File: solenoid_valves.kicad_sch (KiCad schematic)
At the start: 0 parts

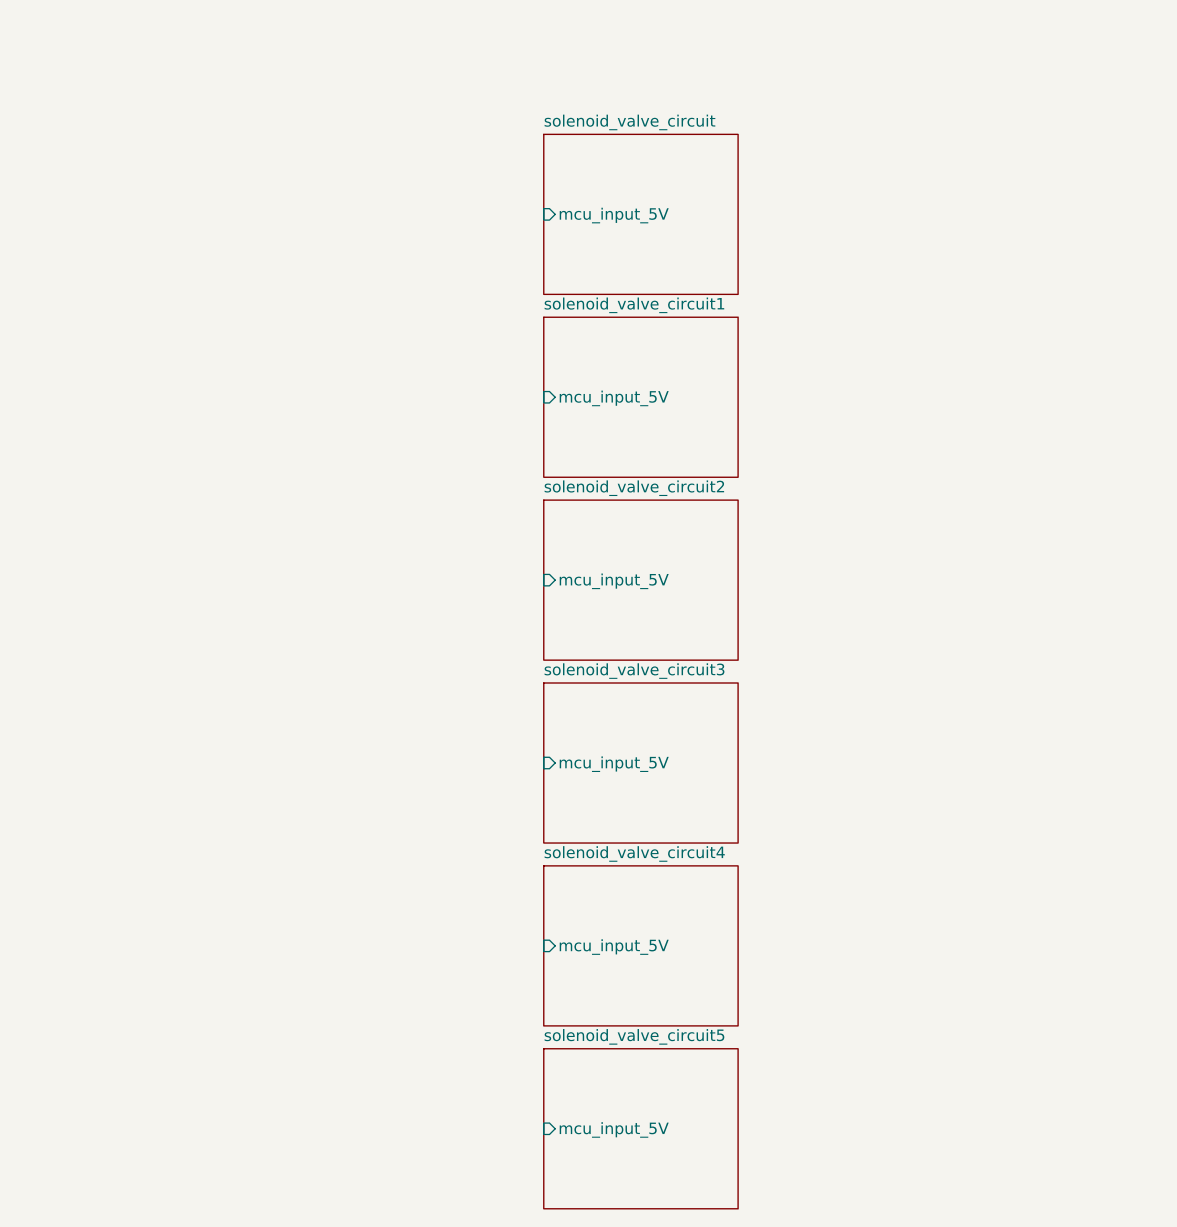
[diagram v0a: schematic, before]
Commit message: added npn in so that GPIO can be 5V or roughly 0V
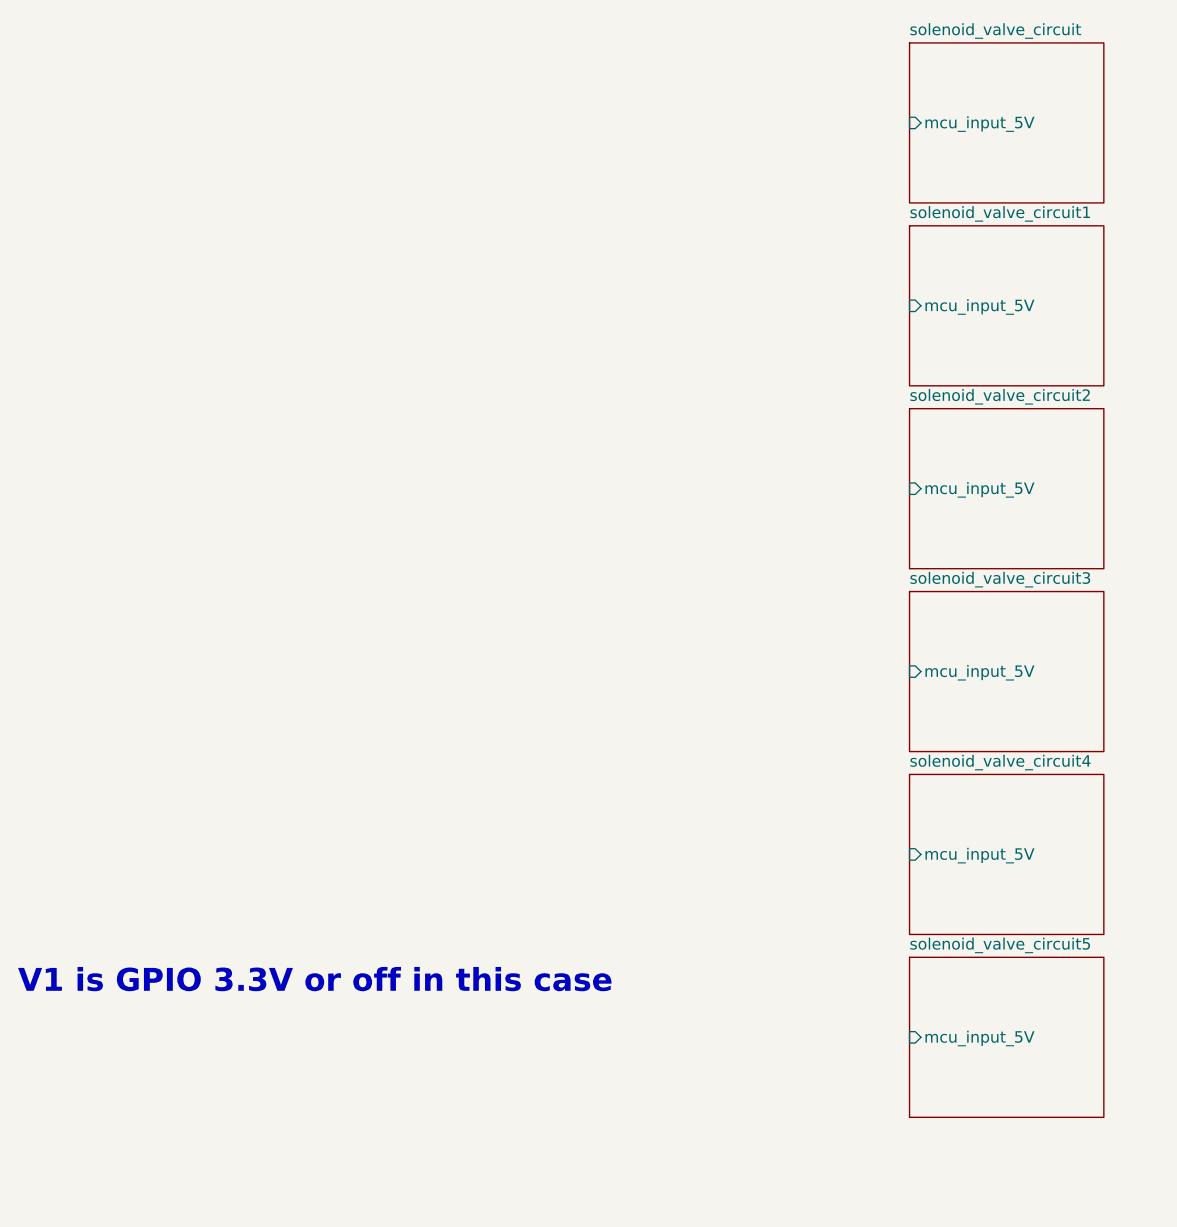
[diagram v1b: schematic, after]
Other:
- note added: "V1 is GPIO 3.3V or off in this case"

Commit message: Added changes to pass ERC check
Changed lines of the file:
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@@
+		)
+	)
+	(wire
+		(pts
+			(xy 132.08 125.73) (xy 133.35 125.73)
+		)
+		(stroke
+			(width 0)
+			(type default)
+		)
+	)
+	(wire
+		(pts
+			(xy 132.08 146.05) (xy 133.35 146.05)
+		)
+		(stroke
+			(width 0)
+			(type default)
+		)
+	)
+	(wire
+		(pts
+			(xy 132.08 85.09) (xy 133.35 85.09)
+		)
+		(stroke
+			(width 0)
+			(type default)
+		)
+	)
+	(wire
+		(pts
+			(xy 132.08 44.45) (xy 133.35 44.45)
+		)
+		(stroke
+			(width 0)
+			(type default)
+		)
+	)
+	(wire
+		(pts
+			(xy 132.08 64.77) (xy 133.35 64.77)
+		)
+		(stroke
+			(width 0)
+			(type default)
+		)
+	)
+	(wire
+		(pts
+			(xy 132.08 105.41) (xy 133.35 105.41)
+		)
+		(stroke
+			(width 0)
+			(type default)
 		)
 	)
@@
 		)
 	)
+	(global_label "Valve3"
+		(shape input)
+		(at 132.08 85.09 180)
+		(fields_autoplaced yes)
+		(effects
+			(font
+				(size 1.27 1.27)
+			)
+			(justify right)
+		)
+		(property "Intersheetrefs" "${INTERSHEET_REFS}"
+			(at 122.9263 85.09 0)
+			(hide yes)
+			(show_name no)
+			(do_not_autoplace no)
+			(effects
+				(font
+					(size 1.27 1.27)
+				)
+				(justify right)
+			)
+		)
+	)
+	(global_label "Valve5"
+		(shape input)
+		(at 132.08 125.73 180)
+		(fields_autoplaced yes)
+		(effects
+			(font
+				(size 1.27 1.27)
+			)
+			(justify right)
+		)
+		(property "Intersheetrefs" "${INTERSHEET_REFS}"
+			(at 122.9263 125.73 0)
+			(hide yes)
+			(show_name no)
+			(do_not_autoplace no)
+			(effects
+				(font
+					(size 1.27 1.27)
+				)
+				(justify right)
+			)
+		)
+	)
+	(global_label "Valve4"
+		(shape input)
+		(at 132.08 105.41 180)
+		(fields_autoplaced yes)
+		(effects
+			(font
+				(size 1.27 1.27)
+			)
+			(justify right)
+		)
+		(property "Intersheetrefs" "${INTERSHEET_REFS}"
+			(at 122.9263 105.41 0)
+			(hide yes)
+			(show_name no)
+			(do_not_autoplace no)
+			(effects
+				(font
+					(size 1.27 1.27)
+				)
+				(justify right)
+			)
+		)
+	)
+	(global_label "Valve2"
+		(shape input)
+		(at 132.08 64.77 180)
+		(fields_autoplaced yes)
+		(effects
+			(font
+				(size 1.27 1.27)
+			)
+			(justify right)
+		)
+		(property "Intersheetrefs" "${INTERSHEET_REFS}"
+			(at 122.9263 64.77 0)
+			(hide yes)
+			(show_name no)
+			(do_not_autoplace no)
+			(effects
+				(font
+					(size 1.27 1.27)
+				)
+				(justify right)
+			)
+		)
+	)
+	(global_label "Valve6"
+		(shape input)
+		(at 132.08 146.05 180)
+		(fields_autoplaced yes)
+		(effects
+			(font
+				(size 1.27 1.27)
+			)
+			(justify right)
+		)
+		(property "Intersheetrefs" "${INTERSHEET_REFS}"
+			(at 122.9263 146.05 0)
+			(hide yes)
+			(show_name no)
+			(do_not_autoplace no)
+			(effects
+				(font
+					(size 1.27 1.27)
+				)
+				(justify right)
+			)
+		)
+	)
+	(global_label "Valve1"
+		(shape input)
+		(at 132.08 44.45 180)
+		(fields_autoplaced yes)
+		(effects
+			(font
+				(size 1.27 1.27)
+			)
+			(justify right)
+		)
+		(property "Intersheetrefs" "${INTERSHEET_REFS}"
+			(at 122.9263 44.45 0)
+			(hide yes)
+			(show_name no)
+			(do_not_autoplace no)
+			(effects
+				(font
+					(size 1.27 1.27)
+				)
+				(justify right)
+			)
+		)
+	)
